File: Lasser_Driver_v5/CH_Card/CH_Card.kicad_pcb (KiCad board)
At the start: 2 copper layers, 160 x 100 mm, 145 parts, among them J1 DIN41612_M_universal, Q13 IRL540N, Q14 IRF9540N, Q17 IRL540N, Q18 IRF9540N, Q19 DMN3404L, U101 AD5696R, U102 ADS1115, U103 PCA9538, U104 ADG419BRM, U105 ADG419BRM, U17 OPA192IDBVR, U19 OPA192IDBVR, U21 OPA551U, U22 OPA192IDBVR, U24 OPA192IDBVR, U26 ADG419BRM, U28 INA828, U32 INA828

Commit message: Progress on laying out the laser PCB
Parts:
- J_BTF1: value DFB1550LP #1 Socket -> Butterfly laser-head harness (off-board mount); footprint Connector_PinSocket_2.54mm:PinSocket_2x07_P2.54mm_Vertical -> Connector_PinHeader_2.54mm:PinHeader_2x07_P2.54mm_Vertical
- R68, R76: value 47R prot -> 10mR link (was 47R - TEC path); footprint Resistor_SMD:R_0805_2012Metric_Pad1.20x1.40mm_HandSolder -> Resistor_SMD:R_2512_6332Metric
- R73: value 47R prot -> 0R link (was 47R - laser path)
- R74: value 47R prot -> 0R link (was 47R - laser path); moved to B.Cu
- R_bias1: value 100k PD bias -> 20k 0.1% PD bias; footprint Resistor_SMD:R_0805_2012Metric_Pad1.20x1.40mm_HandSolder -> Resistor_SMD:R_0805_2012Metric
- moved C136 206.0 mm to (239.8, 118.5)
- moved C146 205.5 mm to (239.8, 126.0)
- moved C117 193.4 mm to (215.8, 160.0)
- moved C120 187.6 mm to (207.8, 163.8), turned to -90 degrees
- moved C119 183.3 mm to (203.5, 160.5), turned to 180 degrees
- moved C70 178.8 mm to (203.2, 124.5), turned to 90 degrees
- moved U_TIA1 173.2 mm to (252.1, 120.8)
- moved U_TIA2 173.2 mm to (252.1, 127.4)
- moved C66 172.4 mm to (196.0, 125.5)
- moved C135 162.4 mm to (192.1, 131.2)
- moved C145 157.9 mm to (192.1, 138.8)
- moved C116 156.8 mm to (179.2, 153.8), turned to -90 degrees
- moved U28 154.2 mm to (236.3, 122.3)
- moved C68 149.9 mm to (174.2, 121.1), turned to 180 degrees
- moved C158 146.3 mm to (189.6, 117.3), turned to 180 degrees
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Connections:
- J_BTF1 pad 3: /unconnected-(J_BTF1-NC-Pad3) -> GND
- J_BTF1 pad 4: /unconnected-(J_BTF1-NC-Pad4) -> /MPD_K
- R62 pad 2: /TEC_BTF_N -> unconnected-(R62-Pad2)
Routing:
- net +6V_TEC: track 0.00 -> 220.5 mm, vias 0 -> 4
- net -6V_TEC: track 0.00 -> 209.3 mm, vias 0 -> 4
- net /N_Q13_S: track 0.00 -> 119.1 mm, vias 0 -> 2
- net /N_U21__: track 0.00 -> 115.7 mm
- net /TEC_BTF_N: track 0.00 -> 61.8 mm
- net 3V3_DIG: track 0.00 -> 57.4 mm, vias 0 -> 2
- net /N_Q17_S: track 0.00 -> 50.5 mm
- net /N_D20_K: track 0.00 -> 38.4 mm, vias 0 -> 1
- net /BTF_LASER_K: track 0.00 -> 37.7 mm, vias 0 -> 1
- net /N_D21_A: track 0.00 -> 36.8 mm, vias 0 -> 1
- net /N_D16_K: track 0.00 -> 36.4 mm, vias 0 -> 1
- net /N_D17_A: track 0.00 -> 34.3 mm, vias 0 -> 1
- net /BTF_LASER: track 0.00 -> 31.8 mm
- net GA2: track 0.00 -> 30.9 mm, vias 0 -> 1
- net /N_Q19_S: track 0.00 -> 26.0 mm
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
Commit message: Working on the CH pcb layout and routing.
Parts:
- removed R62: DNP Rtrim (shunt scale), Resistor_SMD:R_0805_2012Metric_Pad1.20x1.40mm_HandSolder
- added R78: 100k, Resistor_SMD:R_0805_2012Metric_Pad1.20x1.40mm_HandSolder, F.Cu at (203.2, 128.7)
- J_BTF1: value Butterfly laser-head harness (off-board mount) -> Butterfly harness header - Wurth WR-PHD 2x7 (mates LDM-BUTTERFLY)
- moved C152 142.7 mm to (181.8, 125.0)
- moved C153 140.3 mm to (178.8, 135.1)
- moved C_NTC1 121.3 mm to (167.8, 137.4), turned to -90 degrees
- moved C113 117.1 mm to (141.6, 127.0)
- moved C160 116.8 mm to (160.5, 95.7)
- moved C161 116.8 mm to (160.5, 98.7)
- moved C123 107.3 mm to (136.1, 128.0), turned to 90 degrees
- moved C114 104.5 mm to (128.9, 130.2), turned to 90 degrees
- moved R_f1 98.1 mm to (176.0, 121.9)
- moved C138 97.7 mm to (131.0, 123.5), turned to -90 degrees
- moved R_f2 92.0 mm to (172.7, 132.0)
- moved R118 92.0 mm to (177.0, 110.6)
- moved C148 90.5 mm to (129.2, 115.0), turned to 90 degrees
- moved C162 89.0 mm to (77.8, 118.6), turned to -90 degrees
- moved R_bias1 88.8 mm to (170.6, 129.2), turned to -90 degrees
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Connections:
- U_TIA1 pad 1: (no net) -> unconnected-(U_TIA1-NC-Pad1)
- U_TIA1 pad 5: (no net) -> unconnected-(U_TIA1-NC-Pad5)
- U_TIA1 pad 8: (no net) -> unconnected-(U_TIA1-NC-Pad8)
- U_TIA2 pad 1: (no net) -> unconnected-(U_TIA2-NC-Pad1)
- U_TIA2 pad 5: (no net) -> unconnected-(U_TIA2-NC-Pad5)
- U_TIA2 pad 8: (no net) -> unconnected-(U_TIA2-NC-Pad8)
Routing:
- net 3V3: track 0.00 -> 270.7 mm, vias 0 -> 16
- net +15V: track 9.62 -> 217.5 mm, vias 0 -> 12
- net -15V: track 17.6 -> 210.4 mm, vias 0 -> 21
- net GND: track 0.00 -> 174.8 mm, vias 0 -> 173
- net +5V_LASER: track 3.16 -> 146.0 mm, vias 0 -> 2
- net MOD_DRV: track 0.00 -> 142.5 mm, vias 0 -> 7
- net 5Vref: track 0.00 -> 119.6 mm, vias 0 -> 3
- net GA0: track 18.7 -> 132.5 mm, vias 3 -> 7
- net +5V: track 1.76 -> 113.7 mm, vias 0 -> 4
- net NTC_A: track 0.00 -> 108.4 mm, vias 0 -> 4
- net FAULT_n: track 0.00 -> 97.8 mm, vias 0 -> 2
- net TEC_VZERO: track 0.00 -> 96.5 mm, vias 0 -> 7
- net /TEC_BTF_P: track 2.55 -> 82.6 mm, vias 0 -> 2
- net HB_FAULT_LOC: track 0.00 -> 77.1 mm, vias 0 -> 2
- net SDA: track 8.32 -> 78.6 mm, vias 0 -> 6
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- added copper zone on F.Cu, net -6V_TEC
- added copper zone on B.Cu, net GND
- added copper zone on F.Cu, net GND
- added copper zone on In1.Cu, net GND
- added copper zone on B.Cu, net PGND_TEC
- added copper zone on F.Cu, net PGND_TEC
- added copper zone on In1.Cu, net PGND_TEC
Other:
- copper layers 2 -> 4

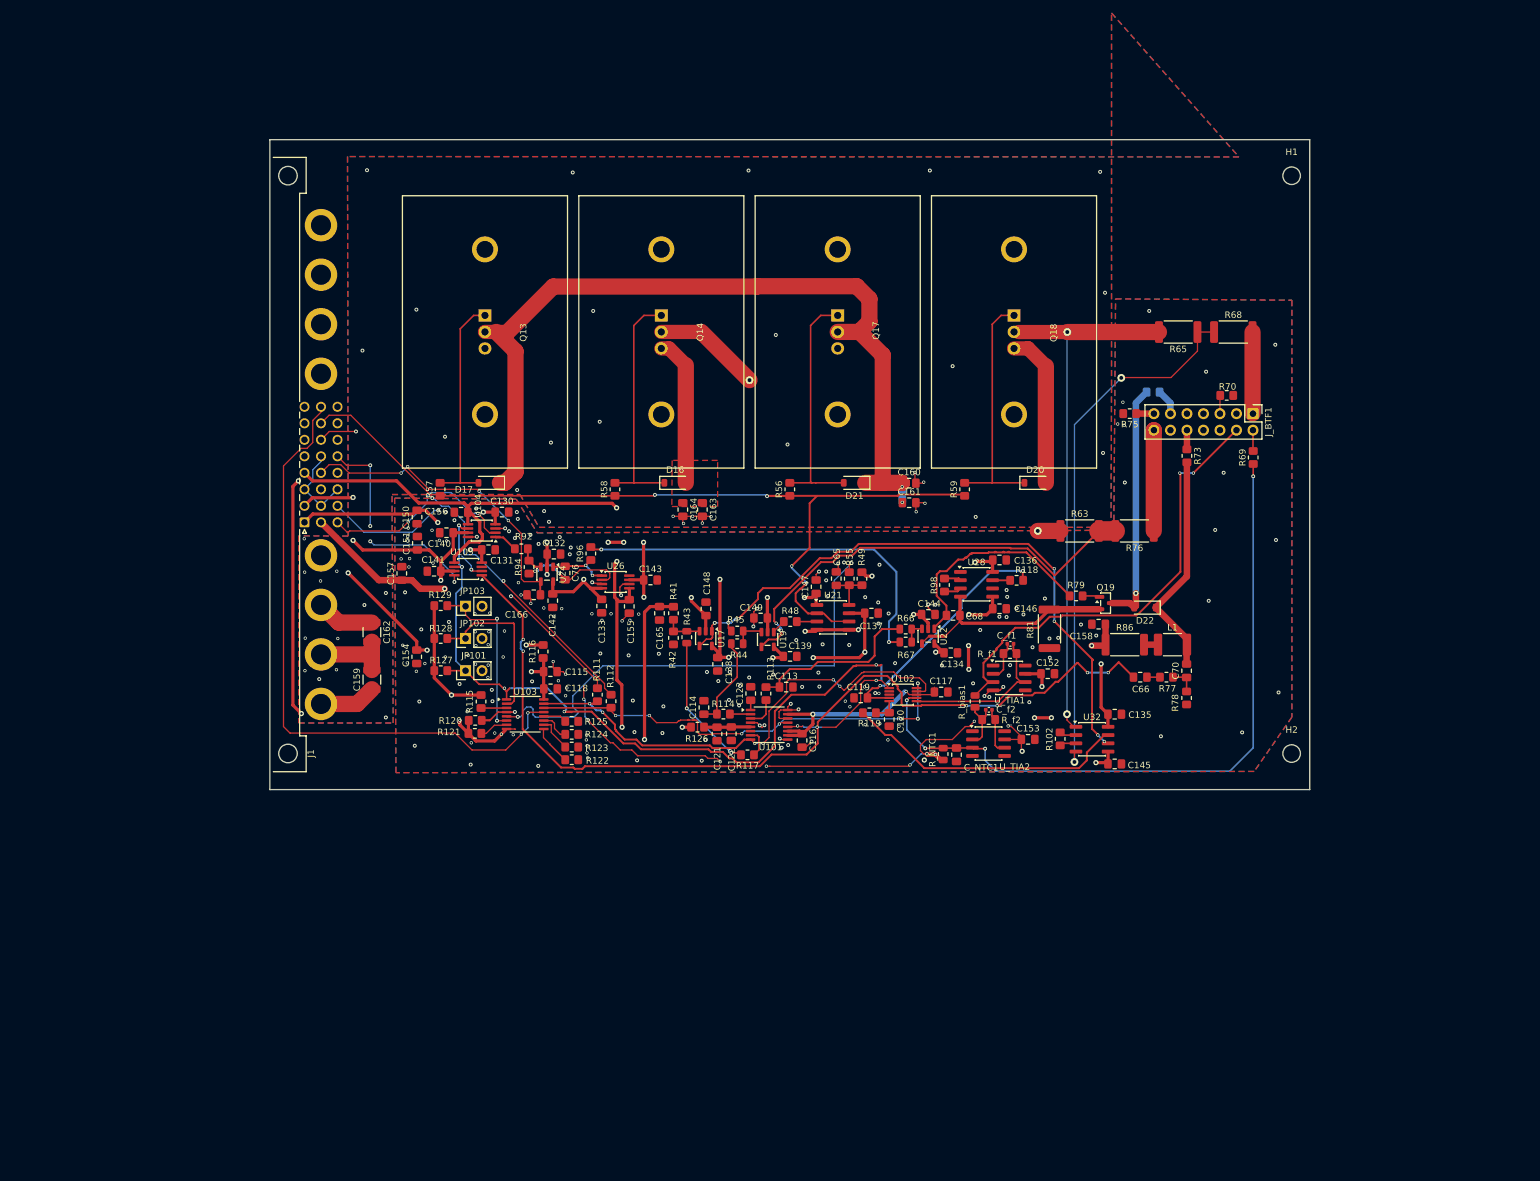
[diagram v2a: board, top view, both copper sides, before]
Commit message: Changed CH card to 6 layer. Added single pt grnd.
CH card is now layed out cleanly with 6 layers.
Added a single point connection with surge protection to the backplane.
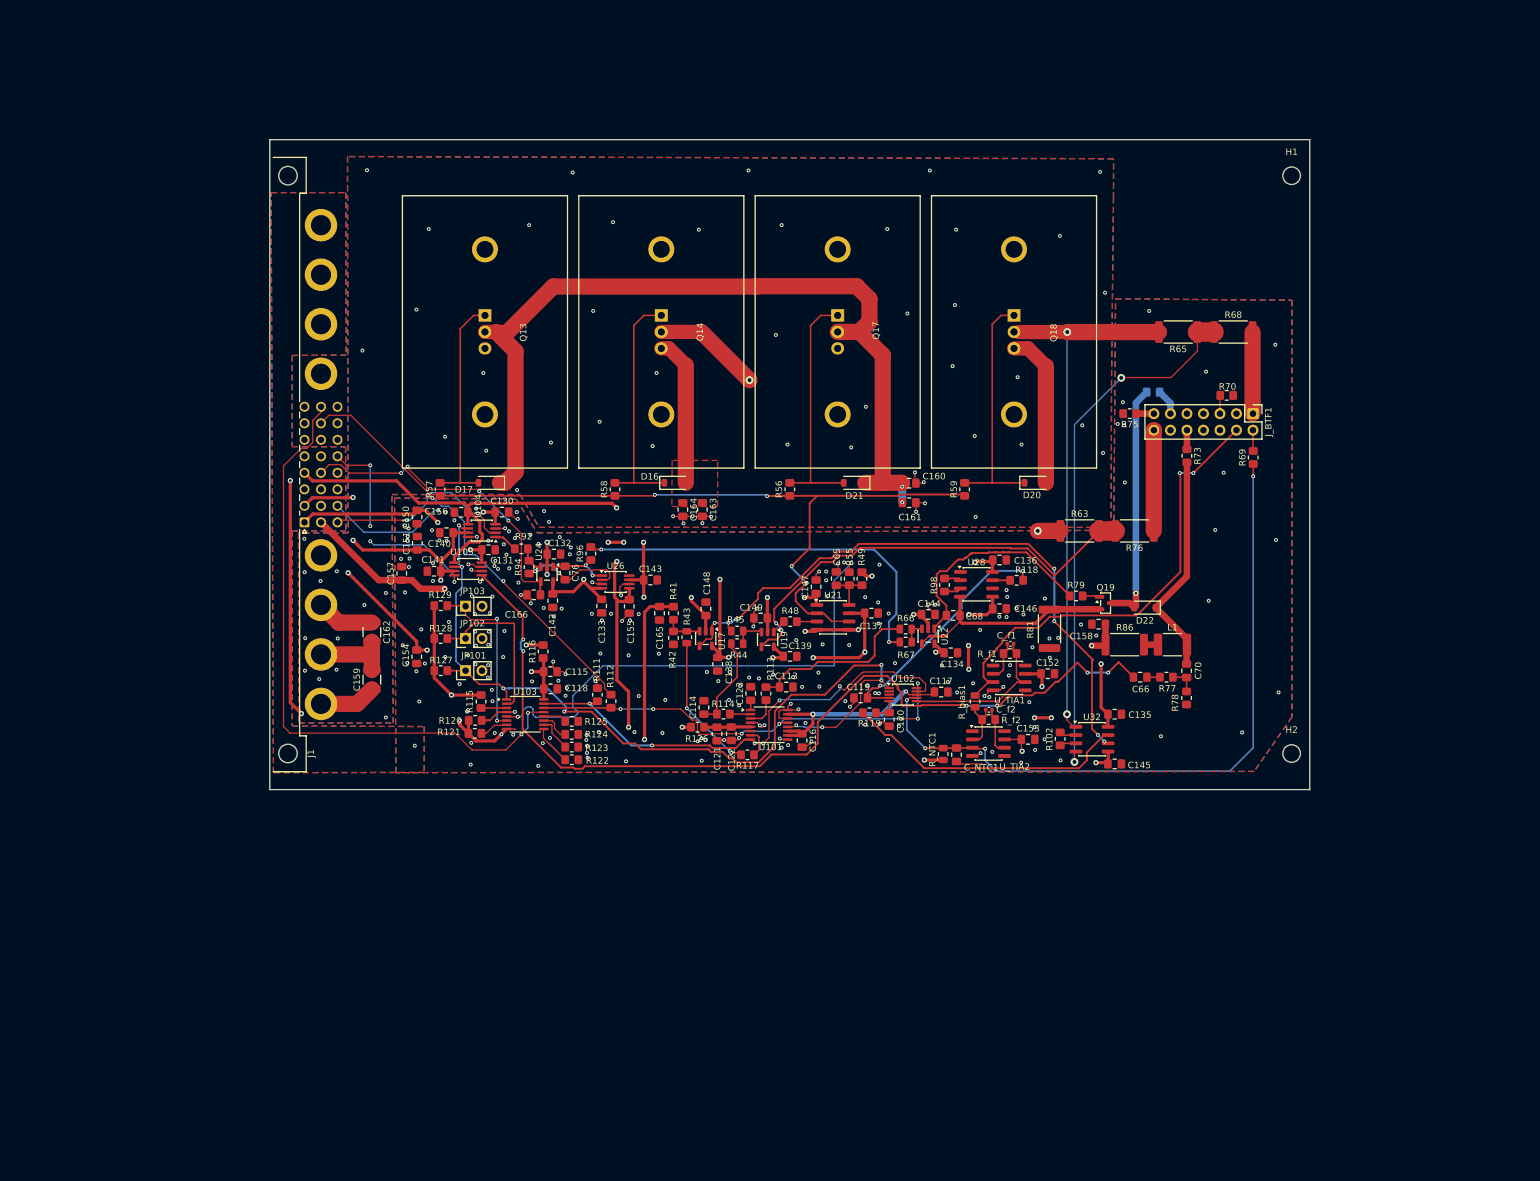
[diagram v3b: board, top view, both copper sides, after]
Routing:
- net GND: track 174.8 -> 62.3 mm, vias 173 -> 205
- net 3V3: track 270.7 -> 189.1 mm, vias 16 -> 7
- net GA2: track 99.1 -> 26.4 mm
- net MOD1_BUS: track 34.8 -> 42.3 mm
- net LOCK_EN: track 37.4 -> 43.6 mm
- net MOD_DRV: track 142.5 -> 139.4 mm, vias 7 -> 6
- net GA0: track 132.5 -> 134.9 mm, vias 7 -> 8
- net SDA: track 78.6 -> 76.5 mm
- net -15V: track 210.4 -> 208.6 mm
- net ERR1_BUS: track 31.4 -> 30.1 mm
- net 5Vref: track 119.6 -> 120.7 mm
- net +15V: track 217.5 -> 218.3 mm
- net SDA_BUS: track 63.9 -> 64.4 mm, vias 2 -> 1
- net +5V: track 113.7 -> 113.2 mm
- net PGND_TEC: vias 41 -> 61
- added copper zone on In2.Cu, net GND
- added copper zone on In3.Cu, net GND
- added copper zone on In4.Cu, net GND
- added copper zone on In2.Cu, net PGND_TEC
- added copper zone on In3.Cu, net PGND_TEC
- added copper zone on In4.Cu, net PGND_TEC
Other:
- copper layers 4 -> 6
